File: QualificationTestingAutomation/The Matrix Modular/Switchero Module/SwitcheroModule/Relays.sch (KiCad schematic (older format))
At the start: 13 parts, among them Q1 2N7002DW, U10 TLP3546, U11 TLP3546

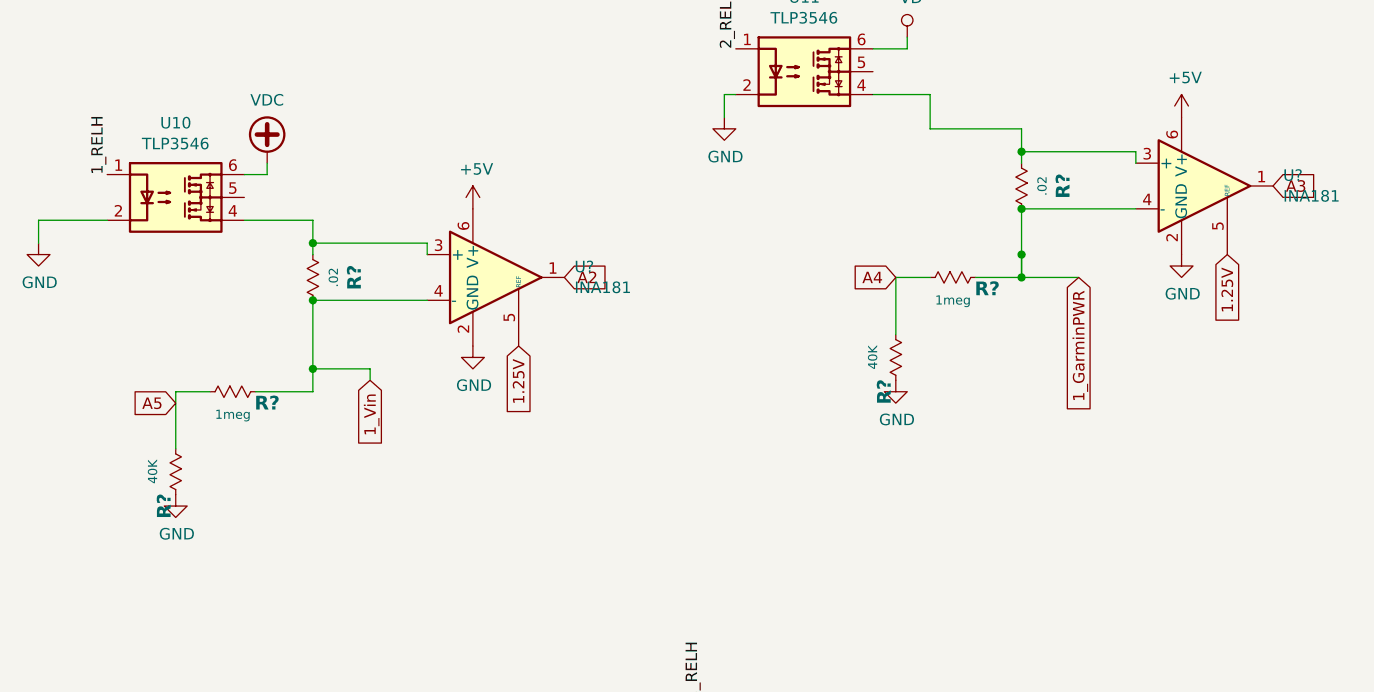
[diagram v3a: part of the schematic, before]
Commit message: Schematic Clean ups the layout needs to be changed
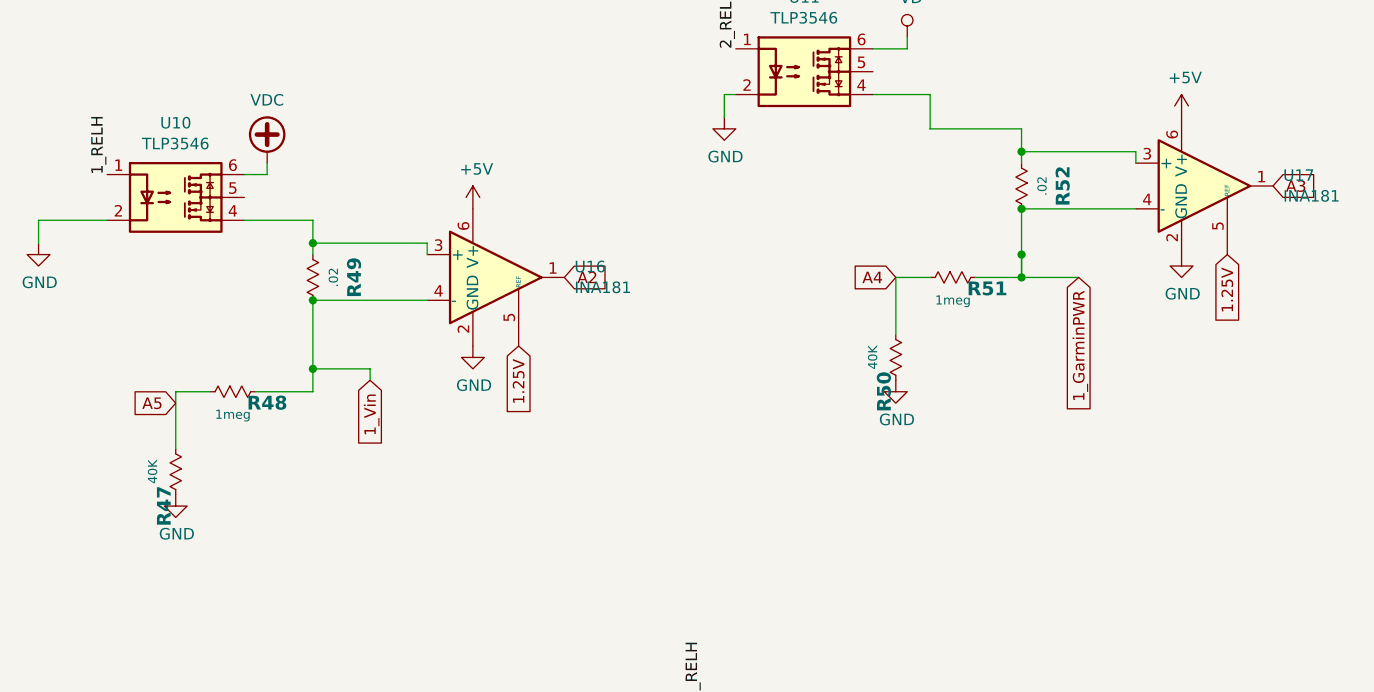
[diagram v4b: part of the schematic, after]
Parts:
- gave numbers to parts that had none: 8
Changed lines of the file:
@@
 	8250 4800 8250 4550
 $Comp
-L Amplifier_Current:INA181 U?
+L Amplifier_Current:INA181 U16
 U 1 1 5C9F45B0
 P 7350 2700
-F 0 "U?" H 7694 2746 50  0000 L CNN
+F 0 "U16" H 7694 2746 50  0000 L CNN
 F 1 "INA181" H 7694 2655 50  0000 L CNN
 F 2 "Package_TO_SOT_SMD:SOT-23-6" H 7400 2750 50  0001 C CNN
@@
 AR Path="/5C90F514/5C94ECF2/5C9FB38A" Ref="R?"  Part="1"
 AR Path="/5C90F514/5C9FB38A" Ref="R?"  Part="1"
-AR Path="/5C8DF48C/5C9FB38A" Ref="R?"  Part="1"
-F 0 "R?" H 6550 2882 60  0000 C CNB
+AR Path="/5C8DF48C/5C9FB38A" Ref="R49"  Part="1"
+F 0 "R49" H 6550 2882 60  0000 C CNB
 F 1 ".02" H 6550 2791 40  0000 C CNN
 F 2 "Resistor_SMD:R_1206_3216Metric_Pad1.42x1.75mm_HandSolder" H 6550 2560 40  0001 C CNN
@@
 Connection ~ 6550 2800
 $Comp
-L power:GND #PWR?
+L power:GND #PWR0219
 U 1 1 5C9FEA7D
 P 7250 3000
-F 0 "#PWR?" H 7250 2750 50  0001 C CNN
+F 0 "#PWR0219" H 7250 2750 50  0001 C CNN
 F 1 "GND" H 7255 2827 50  0000 C CNN
 F 2 "" H 7250 3000 50  0001 C CNN
@@
 1.25V
 $Comp
-L power:+5V #PWR?
+L power:+5V #PWR0220
 U 1 1 5CA34E49
 P 7250 2400
-F 0 "#PWR?" H 7250 2250 50  0001 C CNN
+F 0 "#PWR0220" H 7250 2250 50  0001 C CNN
 F 1 "+5V" H 7265 2573 50  0000 C CNN
 F 2 "" H 7250 2400 50  0001 C CNN
@@
 $EndComp
 $Comp
-L Amplifier_Current:INA181 U?
+L Amplifier_Current:INA181 U17
 U 1 1 5CA395FC
 P 10450 2300
-F 0 "U?" H 10794 2346 50  0000 L CNN
+F 0 "U17" H 10794 2346 50  0000 L CNN
 F 1 "INA181" H 10794 2255 50  0000 L CNN
 F 2 "Package_TO_SOT_SMD:SOT-23-6" H 10500 2350 50  0001 C CNN
@@
 	10150 2400 9650 2400
 $Comp
-L power:GND #PWR?
+L power:GND #PWR0221
 U 1 1 5CA39614
 P 10350 2600
-F 0 "#PWR?" H 10350 2350 50  0001 C CNN
+F 0 "#PWR0221" H 10350 2350 50  0001 C CNN
 F 1 "GND" H 10355 2427 50  0000 C CNN
 F 2 "" H 10350 2600 50  0001 C CNN
@@
 1.25V
 $Comp
-L power:+5V #PWR?
+L power:+5V #PWR0222
 U 1 1 5CA3961C
 P 10350 2000
-F 0 "#PWR?" H 10350 1850 50  0001 C CNN
+F 0 "#PWR0222" H 10350 1850 50  0001 C CNN
 F 1 "+5V" H 10365 2173 50  0000 C CNN
 F 2 "" H 10350 2000 50  0001 C CNN
@@
 AR Path="/5C8DF46C/5CA490DA" Ref="R?"  Part="1"
 AR Path="/5C8DF47A/5CA490DA" Ref="R?"  Part="1"
-AR Path="/5C8DF48C/5CA490DA" Ref="R?"  Part="1"
-F 0 "R?" H 6100 3500 60  0000 C CNB
+AR Path="/5C8DF48C/5CA490DA" Ref="R47"  Part="1"
+F 0 "R47" H 6100 3500 60  0000 C CNB
 F 1 "40K" H 5950 3450 40  0000 C CNN
 F 2 "Resistor_SMD:R_0402_1005Metric" H 5950 3410 40  0001 C CNN
@@
 AR Path="/5C8DF46C/5CA490E2" Ref="R?"  Part="1"
 AR Path="/5C8DF47A/5CA490E2" Ref="R?"  Part="1"
-AR Path="/5C8DF48C/5CA490E2" Ref="R?"  Part="1"
-F 0 "R?" H 6350 3150 60  0000 C CNB
+AR Path="/5C8DF48C/5CA490E2" Ref="R48"  Part="1"
+F 0 "R48" H 6350 3150 60  0000 C CNB
 F 1 "1meg" H 6200 3100 40  0000 C CNN
 F 2 "Resistor_SMD:R_0402_1005Metric" H 6200 3060 40  0001 C CNN
@@
 P 5950 3650
 AR Path="/5C8DF47A/5CA490ED" Ref="#PWR?"  Part="1"
-AR Path="/5C8DF48C/5CA490ED" Ref="#PWR?"  Part="1"
-F 0 "#PWR?" H 5950 3400 50  0001 C CNN
+AR Path="/5C8DF48C/5CA490ED" Ref="#PWR0225"  Part="1"
+F 0 "#PWR0225" H 5950 3400 50  0001 C CNN
 F 1 "GND" H 5955 3477 50  0000 C CNN
 F 2 "" H 5950 3650 50  0001 C CNN
@@
 AR Path="/5C8DF46C/5CA50492" Ref="R?"  Part="1"
 AR Path="/5C8DF47A/5CA50492" Ref="R?"  Part="1"
-AR Path="/5C8DF48C/5CA50492" Ref="R?"  Part="1"
-F 0 "R?" H 9250 3000 60  0000 C CNB
+AR Path="/5C8DF48C/5CA50492" Ref="R50"  Part="1"
+F 0 "R50" H 9250 3000 60  0000 C CNB
 F 1 "40K" H 9100 2950 40  0000 C CNN
 F 2 "Resistor_SMD:R_0402_1005Metric" H 9100 2910 40  0001 C CNN
@@
 AR Path="/5C8DF46C/5CA5049A" Ref="R?"  Part="1"
 AR Path="/5C8DF47A/5CA5049A" Ref="R?"  Part="1"
-AR Path="/5C8DF48C/5CA5049A" Ref="R?"  Part="1"
-F 0 "R?" H 9500 2650 60  0000 C CNB
+AR Path="/5C8DF48C/5CA5049A" Ref="R51"  Part="1"
+F 0 "R51" H 9500 2650 60  0000 C CNB
 F 1 "1meg" H 9350 2600 40  0000 C CNN
 F 2 "Resistor_SMD:R_0402_1005Metric" H 9350 2560 40  0001 C CNN
@@
 P 9100 3150
 AR Path="/5C8DF47A/5CA504A0" Ref="#PWR?"  Part="1"
-AR Path="/5C8DF48C/5CA504A0" Ref="#PWR?"  Part="1"
-F 0 "#PWR?" H 9100 2900 50  0001 C CNN
+AR Path="/5C8DF48C/5CA504A0" Ref="#PWR0226"  Part="1"
+F 0 "#PWR0226" H 9100 2900 50  0001 C CNN
 F 1 "GND" H 9105 2977 50  0000 C CNN
 F 2 "" H 9100 3150 50  0001 C CNN
@@
 AR Path="/5C90F514/5C94ECF2/5CA79B2A" Ref="R?"  Part="1"
 AR Path="/5C90F514/5CA79B2A" Ref="R?"  Part="1"
-AR Path="/5C8DF48C/5CA79B2A" Ref="R?"  Part="1"
-F 0 "R?" H 9650 2482 60  0000 C CNB
+AR Path="/5C8DF48C/5CA79B2A" Ref="R52"  Part="1"
+F 0 "R52" H 9650 2482 60  0000 C CNB
 F 1 ".02" H 9650 2391 40  0000 C CNN
 F 2 "Resistor_SMD:R_1206_3216Metric_Pad1.42x1.75mm_HandSolder" H 9650 2160 40  0001 C CNN

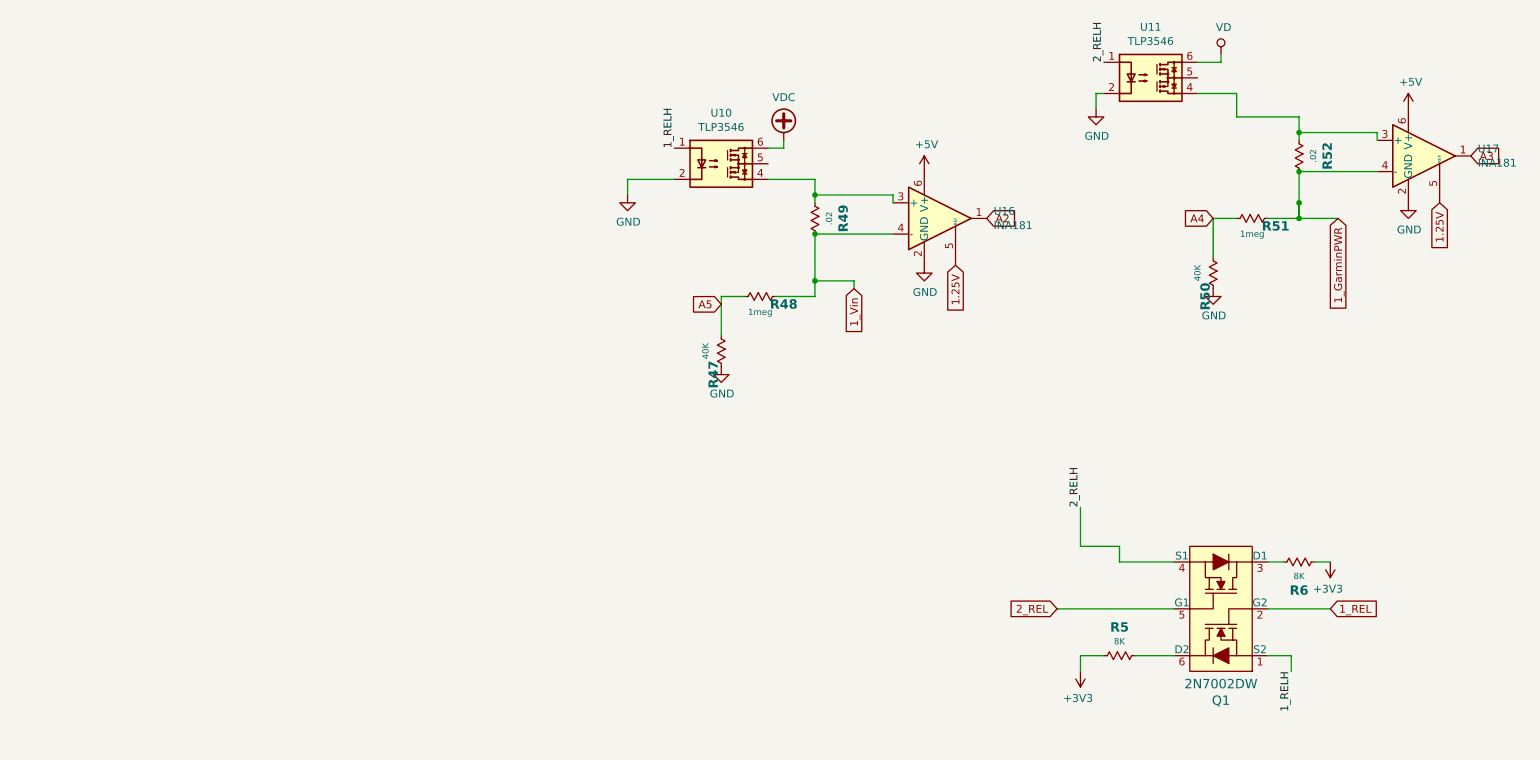
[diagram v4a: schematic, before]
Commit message: IO clean up added the 1v25 reference to Matrix Changed Some of the labels to more legible names.
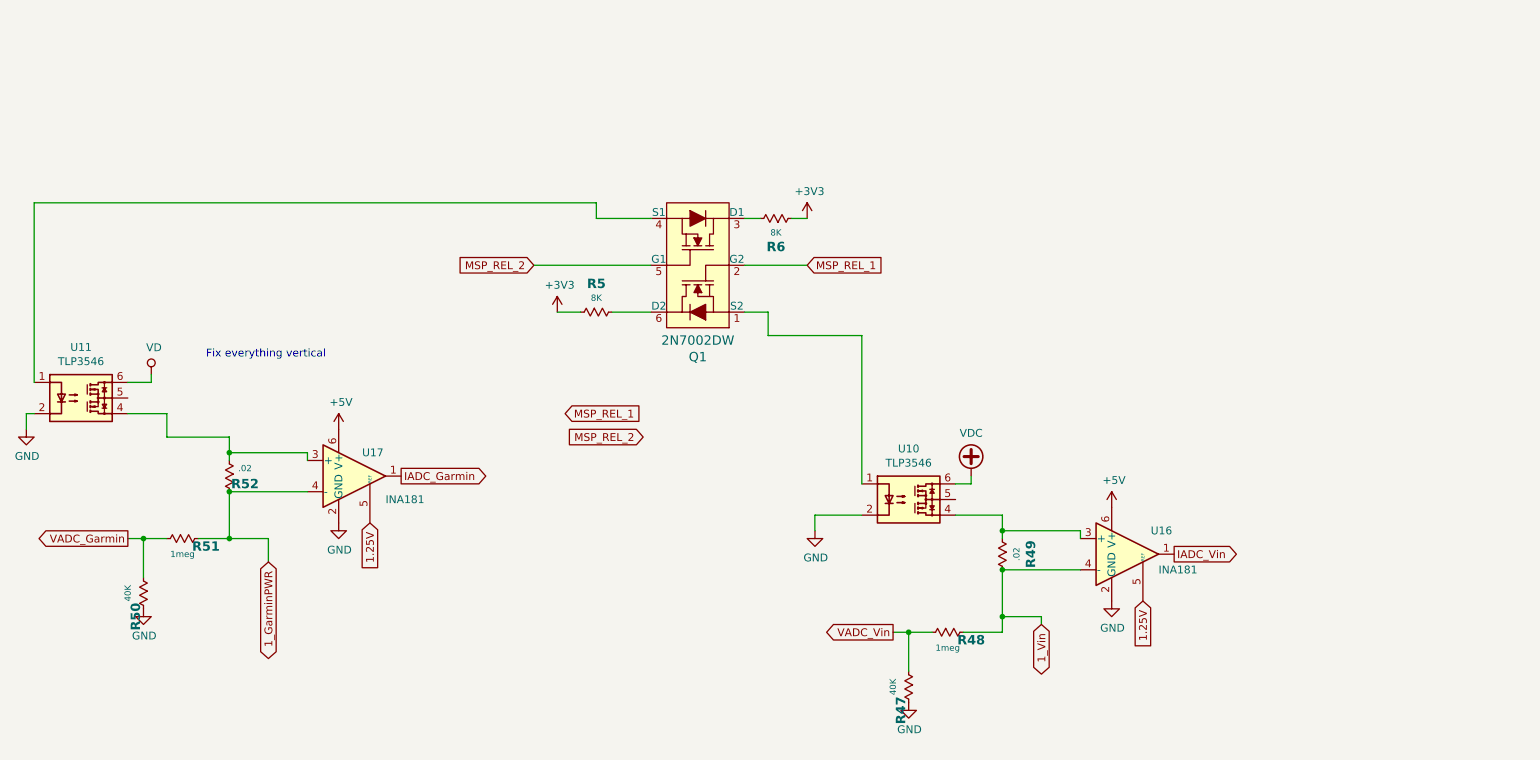
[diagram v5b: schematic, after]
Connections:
- net 1_REL renamed MSP_REL_1
- net 1_RELH: no longer names the net of Q1.1 (S2), U10.1
- net 2_REL renamed MSP_REL_2
- net 2_RELH: no longer names the net of Q1.4 (S1), U11.1
- net A2 renamed IADC_Vin
- net A3 renamed IADC_Garmin
- net A4 renamed VADC_Garmin
- net A5 renamed VADC_Vin
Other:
- note added: "Fix everything vertical"
- moved on the sheet: Q1, R47, R48, R49, R5, R50, R51, R52, R6, U10, U11, U16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

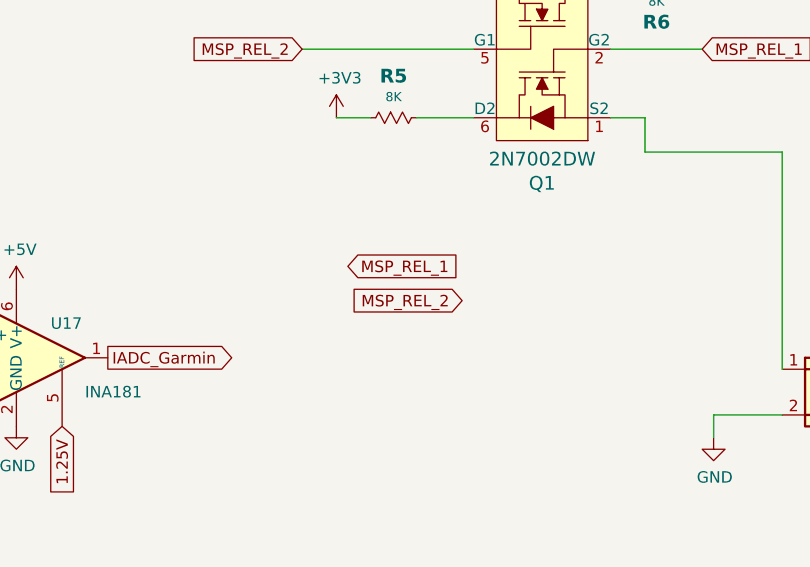
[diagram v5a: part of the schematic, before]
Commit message: Reefero Module PCB design
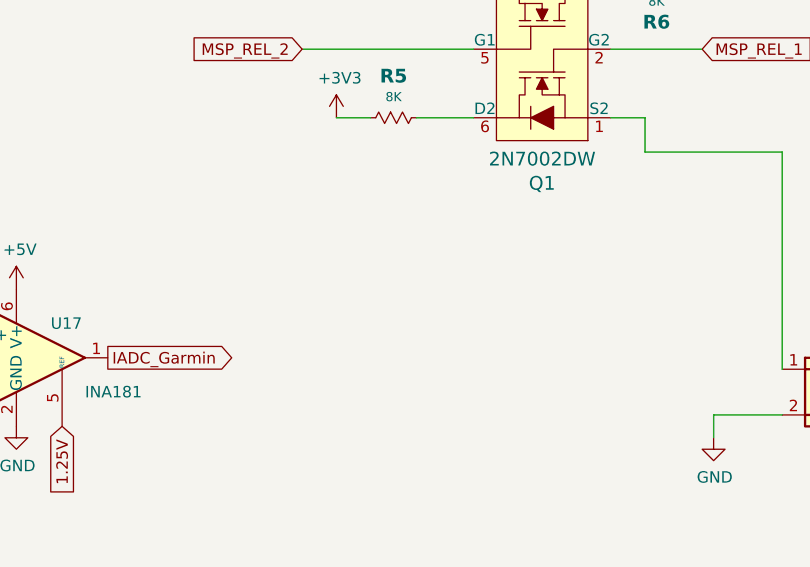
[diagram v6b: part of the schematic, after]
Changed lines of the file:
@@
 Text GLabel 3900 4350 2    50   Output ~ 0
 IADC_Garmin
-Text GLabel 4950 3950 2    50   Input ~ 0
-MSP_REL_1
-Text GLabel 5450 4100 0    50   Input ~ 0
-MSP_REL_2
 $EndSCHEMATC
